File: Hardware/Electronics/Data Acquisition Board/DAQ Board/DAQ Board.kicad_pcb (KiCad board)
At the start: 4 copper layers, 94.7 x 58.9 mm, 133 parts, among them J1 Conn_01x09_Male, J10 ~CS~_TP, J12 START_TP, J14 MID_SUPPLY_TP, J15 AVDD_TP, J16 DVDD_TP, J2 USB_B_Mini, J4 DC Barrel Jack, J5 HC-05 BT Module, J6 ICSP Header, J7 VIN_RAW_TP, Q1 DMP2100U, SW10 SW_SPDT, SW11 SW_SPDT, SW2 SW_DIP_x02, SW3 SW_SPDT, SW4 SW_SPDT, SW5 SW_SPDT, SW6 SW_SPDT, SW7 SW_SPDT, SW8 SW_SPDT, SW9 SW_SPDT, U1 ATmega328P-AU, U2 MCP1755T-5002E_SOT223-5, U3 LM3480-3.3, U4 MCP1755T-5002E_SOT223-5, U5 FT232RL, Y1 16MHz

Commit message: moved some vias
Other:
- board text added: "POW"
- board text added: "STAT"
- board text removed: "POWER"
- board text removed: "STATUS"
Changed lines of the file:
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@@
     (thickness 1.6)
     (drawings 41)
-    (tracks 915)
+    (tracks 917)
     (zones 0)
     (modules 133)
@@
   (layers
     (0 F.Cu signal)
-    (1 In1.Cu power)
-    (2 In2.Cu jumper)
-    (31 B.Cu signal)
-    (32 B.Adhes user)
+    (1 In1.Cu power hide)
+    (2 In2.Cu jumper hide)
+    (31 B.Cu signal hide)
+    (32 B.Adhes user hide)
     (33 F.Adhes user)
-    (34 B.Paste user)
+    (34 B.Paste user hide)
     (35 F.Paste user)
-    (36 B.SilkS user)
+    (36 B.SilkS user hide)
     (37 F.SilkS user)
-    (38 B.Mask user)
+    (38 B.Mask user hide)
     (39 F.Mask user)
-    (40 Dwgs.User user)
-    (41 Cmts.User user)
-    (42 Eco1.User user)
-    (43 Eco2.User user)
-    (44 Edge.Cuts user)
-    (45 Margin user)
-    (46 B.CrtYd user)
+    (40 Dwgs.User user hide)
+    (41 Cmts.User user hide)
+    (42 Eco1.User user hide)
+    (43 Eco2.User user hide)
+    (44 Edge.Cuts user hide)
+    (45 Margin user hide)
+    (46 B.CrtYd user hide)
     (47 F.CrtYd user)
-    (48 B.Fab user)
+    (48 B.Fab user hide)
     (49 F.Fab user hide)
   )
@@
   (module Switches:1825910-6 (layer F.Cu)
     (at 184.54 117.95 270)
-    (fp_text reference PB1 (at -2.95 -0.75 270) (layer F.SilkS)
+    (fp_text reference PB1 (at 3.36 -1.53 270) (layer F.SilkS)
       (effects (font (size 1 1) (thickness 0.15)))
     )
@@
     (tags diode)
     (attr smd)
-    (fp_text reference D6 (at 2.8925 -0.02) (layer F.SilkS)
+    (fp_text reference D6 (at -2.6075 0) (layer F.SilkS)
       (effects (font (size 1 1) (thickness 0.15)))
     )
@@
     (tags capacitor)
     (attr smd)
-    (fp_text reference C13 (at 3.22 -0.02 90) (layer F.SilkS)
+    (fp_text reference C13 (at 3.051482 -0.020428 90) (layer F.SilkS)
       (effects (font (size 1 1) (thickness 0.15)))
     )
@@
     (tags capacitor)
     (attr smd)
-    (fp_text reference C26 (at 0.61 -1.88 -90) (layer F.SilkS)
+    (fp_text reference C26 (at 0.641482 -1.760428 -90) (layer F.SilkS)
       (effects (font (size 1 1) (thickness 0.15)))
     )
@@
     (tags capacitor)
     (attr smd)
-    (fp_text reference C55 (at -1.321415 1.611237) (layer F.SilkS)
+    (fp_text reference C55 (at -1.581843 2.379755) (layer F.SilkS)
       (effects (font (size 1 1) (thickness 0.15)))
     )
@@
     (tags diode)
     (attr smd)
-    (fp_text reference D4 (at 2.81 -0.02) (layer F.SilkS)
+    (fp_text reference D4 (at -2.69 0) (layer F.SilkS)
       (effects (font (size 1 1) (thickness 0.15)))
     )
@@
     (tags diode)
     (attr smd)
-    (fp_text reference D5 (at 2.83 -0.01) (layer F.SilkS)
+    (fp_text reference D5 (at -2.67 0.01) (layer F.SilkS)
       (effects (font (size 1 1) (thickness 0.15)))
     )
@@
     (descr "Barrel Jack, 2.0mm ID, 5.5mm OD, 24V, 8A, no switch, https://www.cui.com/product/resource/pj-063ah.pdf")
     (tags "barrel jack cui dc power")
-    (fp_text reference J4 (at 6.760428 12.191482 270) (layer F.SilkS)
+    (fp_text reference J4 (at -6.729572 0.261482 270) (layer F.SilkS)
       (effects (font (size 1 1) (thickness 0.15)))
     )
@@
     (tags SOT-23)
     (attr smd)
-    (fp_text reference Q1 (at 2.84 -0.63) (layer F.SilkS)
+    (fp_text reference Q1 (at 2.889572 -1.251482) (layer F.SilkS)
       (effects (font (size 1 1) (thickness 0.15)))
     )
@@
     (effects (font (size 1 1) (thickness 0.15)))
   )
-  (gr_text USB (at 140.790428 106.771482 180) (layer F.SilkS)
+  (gr_text USB (at 138.14 106.67) (layer F.SilkS)
     (effects (font (size 1 1) (thickness 0.15) italic) (justify left))
   )
-  (gr_text "BT\n" (at 135.420428 106.821482 180) (layer F.SilkS)
+  (gr_text "BT\n" (at 133.08 106.75) (layer F.SilkS)
     (effects (font (size 1 1) (thickness 0.15) italic) (justify left))
   )
@@
     (effects (font (size 1.5 1.5) (thickness 0.3)))
   )
-  (gr_text POWER (at 174.610428 111.591482) (layer F.SilkS)
+  (gr_text POW (at 184.403285 111.631482) (layer F.SilkS)
     (effects (font (size 1.5 1.5) (thickness 0.3)))
   )
-  (gr_text STATUS (at 174.450428 113.741482) (layer F.SilkS)
+  (gr_text STAT (at 184.510428 113.781482) (layer F.SilkS)
     (effects (font (size 1.5 1.5) (thickness 0.3)))
   )
@@
     (effects (font (size 1.5 1.5) (thickness 0.3)))
   )
-  (gr_text ADC (at 176.200428 115.901482) (layer F.SilkS)
+  (gr_text ADC (at 184.153285 115.941482) (layer F.SilkS)
     (effects (font (size 1.5 1.5) (thickness 0.3)))
   )
   (via (at 188.02 116.62) (size 0.8) (drill 0.4) (layers F.Cu B.Cu) (net 0))
+  (via (at 149.61 94.62) (size 0.8) (drill 0.4) (layers F.Cu B.Cu) (net 13))
+  (via (at 145.61 94.62) (size 0.8) (drill 0.4) (layers F.Cu B.Cu) (net 13))
+  (via (at 181.74 86.43) (size 0.8) (drill 0.4) (layers F.Cu B.Cu) (net 13))
+  (via (at 177.74 86.43) (size 0.8) (drill 0.4) (layers F.Cu B.Cu) (net 13))
   (segment (start 181.969687 72.654723) (end 181.972928 72.651482) (width 0.5) (layer F.Cu) (net 1))
   (segment (start 181.969687 74.238641) (end 181.969687 72.654723) (width 0.5) (layer F.Cu) (net 1))
@@
   (via (at 216.02 72.62) (size 0.8) (drill 0.4) (layers F.Cu B.Cu) (net 13))
   (via (at 220.02 72.62) (size 0.8) (drill 0.4) (layers F.Cu B.Cu) (net 13))
-  (via (at 136.02 76.62) (size 0.8) (drill 0.4) (layers F.Cu B.Cu) (net 13))
+  (via (at 137.59 76.5) (size 0.8) (drill 0.4) (layers F.Cu B.Cu) (net 13))
   (via (at 144.02 76.62) (size 0.8) (drill 0.4) (layers F.Cu B.Cu) (net 13))
   (via (at 148.02 76.62) (size 0.8) (drill 0.4) (layers F.Cu B.Cu) (net 13))
@@
   (via (at 220.02 100.62) (size 0.8) (drill 0.4) (layers F.Cu B.Cu) (net 13))
   (via (at 136.02 104.62) (size 0.8) (drill 0.4) (layers F.Cu B.Cu) (net 13))
-  (via (at 144.02 104.62) (size 0.8) (drill 0.4) (layers F.Cu B.Cu) (net 13))
   (via (at 160.02 104.62) (size 0.8) (drill 0.4) (layers F.Cu B.Cu) (net 13))
   (via (at 164.02 104.62) (size 0.8) (drill 0.4) (layers F.Cu B.Cu) (net 13))
@@
   (via (at 144.02 116.62) (size 0.8) (drill 0.4) (layers F.Cu B.Cu) (net 13))
   (via (at 148.02 116.62) (size 0.8) (drill 0.4) (layers F.Cu B.Cu) (net 13))
-  (via (at 152.02 116.62) (size 0.8) (drill 0.4) (layers F.Cu B.Cu) (net 13))
-  (via (at 156.02 116.62) (size 0.8) (drill 0.4) (layers F.Cu B.Cu) (net 13))
-  (via (at 160.02 116.62) (size 0.8) (drill 0.4) (layers F.Cu B.Cu) (net 13))
-  (via (at 164.02 116.62) (size 0.8) (drill 0.4) (layers F.Cu B.Cu) (net 13))
+  (via (at 151.21 116.58) (size 0.8) (drill 0.4) (layers F.Cu B.Cu) (net 13))
   (via (at 211.84 120.53) (size 0.8) (drill 0.4) (layers F.Cu B.Cu) (net 13))
   (via (at 207.78 116.69) (size 0.8) (drill 0.4) (layers F.Cu B.Cu) (net 13))
@@
   (via (at 135.16 94.83) (size 0.8) (drill 0.4) (layers F.Cu B.Cu) (net 36))
   (via (at 149.130428 104.161482) (size 0.8) (drill 0.4) (layers F.Cu B.Cu) (net 36))
-  (via (at 131.670428 77.141482) (size 0.8) (drill 0.4) (layers F.Cu B.Cu) (net 36))
-  (via (at 128.650428 77.141482) (size 0.8) (drill 0.4) (layers F.Cu B.Cu) (net 36))
+  (via (at 130.22 78.36) (size 0.8) (drill 0.4) (layers F.Cu B.Cu) (net 36))
+  (via (at 127.31 78.59) (size 0.8) (drill 0.4) (layers F.Cu B.Cu) (net 36))
   (via (at 134.770428 79.041482) (size 0.8) (drill 0.4) (layers F.Cu B.Cu) (net 36))
   (via (at 141.670428 81.671482) (size 0.8) (drill 0.4) (layers F.Cu B.Cu) (net 36))
@@
   (segment (start 134.79656 83.505179) (end 134.79656 85.609962) (width 0.5) (layer F.Cu) (net 36))
   (segment (start 131.670428 78.62133) (end 131.671843 78.622745) (width 0.5) (layer F.Cu) (net 36))
-  (segment (start 131.670428 77.141482) (end 131.670428 78.62133) (width 0.5) (layer F.Cu) (net 36))
   (segment (start 128.650428 78.613982) (end 128.680428 78.643982) (width 0.5) (layer F.Cu) (net 36))
-  (segment (start 128.650428 77.141482) (end 128.650428 78.613982) (width 0.5) (layer F.Cu) (net 36))
   (segment (start 147.377928 99.473982) (end 147.390428 99.461482) (width 0.5) (layer F.Cu) (net 36))
   (segment (start 147.377928 101.411482) (end 147.377928 99.473982) (width 0.5) (layer F.Cu) (net 36))
@@
   (segment (start 135.161482 94.831482) (end 135.16 94.83) (width 0.5) (layer F.Cu) (net 36))
   (segment (start 136.342928 94.831482) (end 135.161482 94.831482) (width 0.5) (layer F.Cu) (net 36))
+  (segment (start 127.363982 78.643982) (end 127.31 78.59) (width 0.5) (layer F.Cu) (net 36))
+  (segment (start 128.680428 78.643982) (end 127.363982 78.643982) (width 0.5) (layer F.Cu) (net 36))
+  (segment (start 131.409098 78.36) (end 131.671843 78.622745) (width 0.5) (layer F.Cu) (net 36))
+  (segment (start 130.22 78.36) (end 131.409098 78.36) (width 0.5) (layer F.Cu) (net 36))
   (via (at 152.280428 68.081482) (size 0.8) (drill 0.4) (layers F.Cu B.Cu) (net 37))
   (via (at 186.910428 111.061482) (size 0.8) (drill 0.4) (layers F.Cu B.Cu) (net 37))

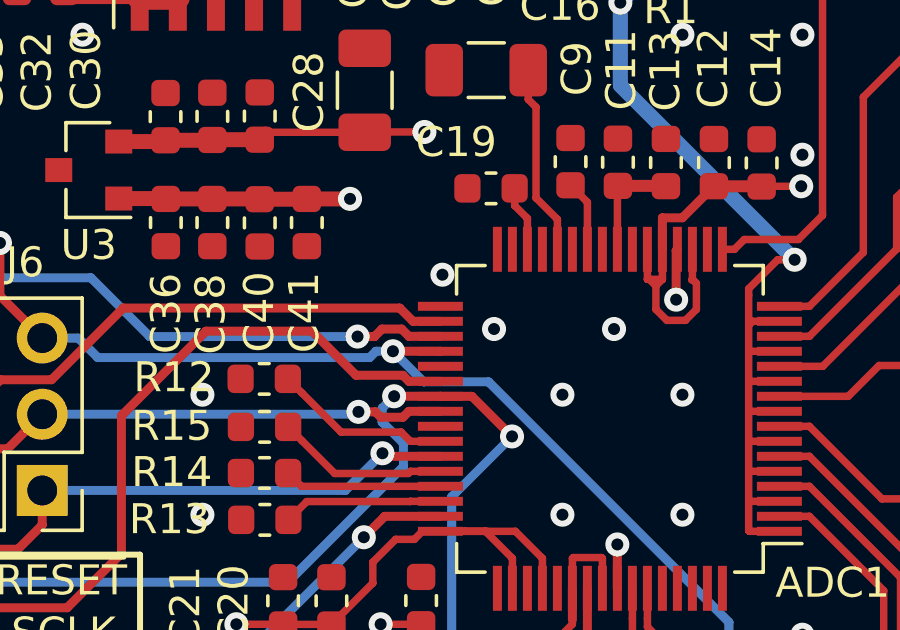
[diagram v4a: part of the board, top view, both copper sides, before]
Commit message: Added pullup to ADS1299 CS pin
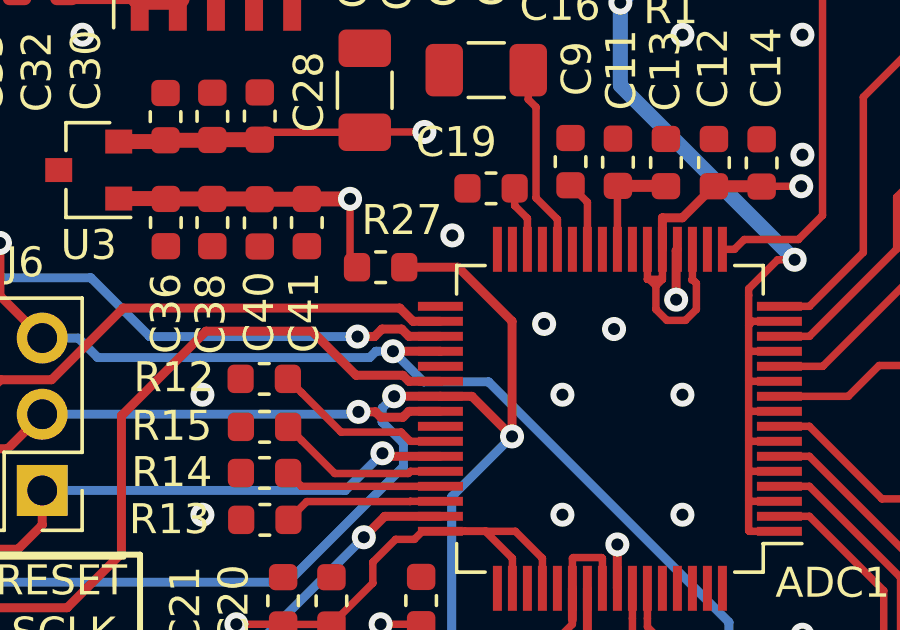
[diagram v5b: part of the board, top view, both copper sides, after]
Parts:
- added R27: 100k, Resistor_SMD:R_0603_1608Metric, F.Cu at (174.0, 84.4)
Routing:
- net /~CS: track 60.5 -> 68.7 mm
- net /ADC1299/DVDD: track 59.8 -> 62.2 mm
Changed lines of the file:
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@@
     (thickness 1.6)
     (drawings 41)
-    (tracks 917)
+    (tracks 922)
     (zones 0)
-    (modules 133)
+    (modules 134)
     (nets 113)
   )
@@
   (layers
     (0 F.Cu signal)
-    (1 In1.Cu power hide)
-    (2 In2.Cu jumper hide)
-    (31 B.Cu signal hide)
-    (32 B.Adhes user hide)
+    (1 In1.Cu power)
+    (2 In2.Cu jumper)
+    (31 B.Cu signal)
+    (32 B.Adhes user)
     (33 F.Adhes user)
-    (34 B.Paste user hide)
+    (34 B.Paste user)
     (35 F.Paste user)
-    (36 B.SilkS user hide)
+    (36 B.SilkS user)
     (37 F.SilkS user)
-    (38 B.Mask user hide)
+    (38 B.Mask user)
     (39 F.Mask user)
-    (40 Dwgs.User user hide)
-    (41 Cmts.User user hide)
-    (42 Eco1.User user hide)
+    (40 Dwgs.User user)
+    (41 Cmts.User user)
+    (42 Eco1.User user)
     (43 Eco2.User user hide)
-    (44 Edge.Cuts user hide)
-    (45 Margin user hide)
-    (46 B.CrtYd user hide)
+    (44 Edge.Cuts user)
+    (45 Margin user)
+    (46 B.CrtYd user)
     (47 F.CrtYd user)
     (48 B.Fab user hide)
@@
     (add_net "/Arduino Nano/VUSB")
   )
+  (module Resistor_SMD:R_0603_1608Metric (layer F.Cu)
+    (at 173.96 84.37)
+    (descr "Resistor SMD 0603 (1608 Metric), square (rectangular) end terminal, IPC_7351 nominal, (Body size source: http://www.tortai-tech.com/upload/download/2011102023233369053.pdf), generated with kicad-footprint-generator")
+    (tags resistor)
+    (attr smd)
+    (fp_text reference R27 (at 0.71 -1.57) (layer F.SilkS)
+      (effects (font (size 1 1) (thickness 0.15)))
+    )
+    (fp_text value 100k (at 0 1.43) (layer F.Fab)
+      (effects (font (size 1 1) (thickness 0.15)))
+    )
+    (fp_line (start -0.8 0.4) (end -0.8 -0.4) (layer F.Fab) (width 0.1))
+    (fp_line (start -0.8 -0.4) (end 0.8 -0.4) (layer F.Fab) (width 0.1))
+    (fp_line (start 0.8 -0.4) (end 0.8 0.4) (layer F.Fab) (width 0.1))
+    (fp_line (start 0.8 0.4) (end -0.8 0.4) (layer F.Fab) (width 0.1))
+    (fp_line (start -0.162779 -0.51) (end 0.162779 -0.51) (layer F.SilkS) (width 0.12))
+    (fp_line (start -0.162779 0.51) (end 0.162779 0.51) (layer F.SilkS) (width 0.12))
+    (fp_line (start -1.48 0.73) (end -1.48 -0.73) (layer F.CrtYd) (width 0.05))
+    (fp_line (start -1.48 -0.73) (end 1.48 -0.73) (layer F.CrtYd) (width 0.05))
+    (fp_line (start 1.48 -0.73) (end 1.48 0.73) (layer F.CrtYd) (width 0.05))
+    (fp_line (start 1.48 0.73) (end -1.48 0.73) (layer F.CrtYd) (width 0.05))
+    (fp_text user %R (at 0 0) (layer F.Fab)
+      (effects (font (size 0.4 0.4) (thickness 0.06)))
+    )
+    (pad 1 smd roundrect (at -0.7875 0) (size 0.875 0.95) (layers F.Cu F.Paste F.Mask) (roundrect_rratio 0.25)
+      (net 28 /ADC1299/DVDD))
+    (pad 2 smd roundrect (at 0.7875 0) (size 0.875 0.95) (layers F.Cu F.Paste F.Mask) (roundrect_rratio 0.25)
+      (net 111 /~CS))
+    (model ${KISYS3DMOD}/Resistor_SMD.3dshapes/R_0603_1608Metric.wrl
+      (at (xyz 0 0 0))
+      (scale (xyz 1 1 1))
+      (rotate (xyz 0 0 0))
+    )
+  )
   (module Capacitor_SMD:C_0603_1608Metric (layer F.Cu)
     (at 141.61 92.75 90)
@@
   (via (at 145.61 94.62) (size 0.8) (drill 0.4) (layers F.Cu B.Cu) (net 13))
   (via (at 181.74 86.43) (size 0.8) (drill 0.4) (layers F.Cu B.Cu) (net 13))
-  (via (at 177.74 86.43) (size 0.8) (drill 0.4) (layers F.Cu B.Cu) (net 13))
+  (via (at 179.41 86.26) (size 0.8) (drill 0.4) (layers F.Cu B.Cu) (net 13))
   (segment (start 181.969687 72.654723) (end 181.972928 72.651482) (width 0.5) (layer F.Cu) (net 1))
   (segment (start 181.969687 74.238641) (end 181.969687 72.654723) (width 0.5) (layer F.Cu) (net 1))
@@
   (via (at 148.02 84.62) (size 0.8) (drill 0.4) (layers F.Cu B.Cu) (net 13))
   (via (at 152.02 84.62) (size 0.8) (drill 0.4) (layers F.Cu B.Cu) (net 13))
-  (via (at 176.02 84.62) (size 0.8) (drill 0.4) (layers F.Cu B.Cu) (net 13))
+  (via (at 176.35 83.31) (size 0.8) (drill 0.4) (layers F.Cu B.Cu) (net 13))
   (via (at 200.02 84.62) (size 0.8) (drill 0.4) (layers F.Cu B.Cu) (net 13))
   (via (at 220.02 84.62) (size 0.8) (drill 0.4) (layers F.Cu B.Cu) (net 13))
@@
   (segment (start 175.952928 93.173482) (end 176.750428 93.173482) (width 0.25) (layer F.Cu) (net 28))
   (segment (start 176.750428 93.173482) (end 177.50293 93.173482) (width 0.25) (layer F.Cu) (net 28))
+  (segment (start 172.940428 84.137928) (end 173.1725 84.37) (width 0.25) (layer F.Cu) (net 28))
+  (segment (start 172.940428 82.091482) (end 172.940428 84.137928) (width 0.25) (layer F.Cu) (net 28))
   (segment (start 180.477928 99.211482) (end 180.477928 97.611482) (width 0.4) (layer F.Cu) (net 29))
   (segment (start 180.852928 97.236482) (end 180.852928 95.073482) (width 0.3) (layer F.Cu) (net 29))
@@
   (segment (start 172.924315 106.56) (end 172.204314 107.280001) (width 0.3) (layer F.Cu) (net 111))
   (segment (start 173.49 106.56) (end 172.924315 106.56) (width 0.3) (layer F.Cu) (net 111))
+  (segment (start 178.340428 86.170428) (end 178.340428 90.010982) (width 0.3) (layer F.Cu) (net 111))
+  (segment (start 174.7475 84.37) (end 176.54 84.37) (width 0.3) (layer F.Cu) (net 111))
+  (segment (start 176.54 84.37) (end 178.340428 86.170428) (width 0.3) (layer F.Cu) (net 111))
   (via (at 161.270428 83.561482) (size 0.8) (drill 0.4) (layers F.Cu B.Cu) (net 112))
   (via (at 174.370428 87.171482) (size 0.8) (drill 0.4) (layers F.Cu B.Cu) (net 112))
@@
     (polygon
       (pts
-        (xy 222.010428 126.601482) (xy 171.550428 126.671482) (xy 171.530428 103.081482) (xy 164.780428 102.771482) (xy 164.730428 85.191482)
+        (xy 222.010428 126.601482) (xy 171.550428 126.671482) (xy 171.530428 103.081482) (xy 164.84 103.1) (xy 164.730428 85.191482)
         (xy 158.240428 85.291482) (xy 158.150428 78.851482) (xy 148.340428 79.001482) (xy 148.340428 65.591482) (xy 162.090428 65.581482)
         (xy 162.110428 76.761482) (xy 164.220428 76.721482) (xy 164.260428 83.621482) (xy 168.240428 83.631482) (xy 168.170428 85.511482)
@@
     (polygon
       (pts
-        (xy 166.92 108.12) (xy 178.44 108.06) (xy 178.41 131.32) (xy 166.98 131.4)
+        (xy 165.74 108.1) (xy 178.44 108.06) (xy 178.41 131.32) (xy 165.8 131.38)
       )
     )

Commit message: ran DRC
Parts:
- added J11: Conn_01x01_Male, Sparker:DIN 42802-1, F.Cu at (226.1, 96.4)
- added J13: Conn_01x01_Male, Sparker:DIN 42802-1, F.Cu at (217.2, 90.3)
- added J17: Conn_01x01_Male, Sparker:DIN 42802-1, F.Cu at (226.1, 84.3)
- added J18: Conn_01x01_Male, Sparker:DIN 42802-1, F.Cu at (217.2, 78.2)
- added J19: Conn_01x01_Male, Sparker:DIN 42802-1, F.Cu at (226.1, 72.2)
- added J3: Conn_01x01_Male, Sparker:DIN 42802-1, F.Cu at (217.2, 114.5)
- added J8: Conn_01x01_Male, Sparker:DIN 42802-1, F.Cu at (226.1, 108.5)
- added J9: Conn_01x01_Male, Sparker:DIN 42802-1, F.Cu at (217.2, 102.4)
- F1: value 0251004.NRT1L -> 025101.5MAT1L
- J1: value Conn_01x09_Male -> Conn_01x01_Male; footprint Connectors:TE-5-103669-8 -> Sparker:DIN 42802-1
- moved J1 22.4 mm to (226.1, 120.6)
- moved MH4 11.2 mm to (148.9, 123.0)
- moved LOGO1 4.62 mm to (207.6, 114.7)
- moved MH1 1.15 mm to (216.1, 123.0)
- moved MH2 1.07 mm to (216.2, 70.0)
- moved MH3 0.82 mm to (130.4, 70.0)
- turned J10 to 90 degrees
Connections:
- SW10 pad 3: Net-(J1-Pad8) -> Net-(J18-Pad1)
- SW11 pad 3: Net-(J1-Pad9) -> Net-(J19-Pad1)
- SW4 pad 3: Net-(J1-Pad2) -> Net-(J3-Pad1)
- SW5 pad 3: Net-(J1-Pad3) -> Net-(J8-Pad1)
- SW6 pad 3: Net-(J1-Pad4) -> Net-(J9-Pad1)
- SW7 pad 3: Net-(J1-Pad5) -> Net-(J11-Pad1)
- SW8 pad 3: Net-(J1-Pad6) -> Net-(J13-Pad1)
- SW9 pad 3: Net-(J1-Pad7) -> Net-(J17-Pad1)
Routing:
- net Net-(J8-Pad1): track 0.00 -> 21.8 mm
- net Net-(J11-Pad1): track 0.00 -> 21.2 mm
- net Net-(J17-Pad1): track 0.00 -> 19.2 mm
- net Net-(J19-Pad1): track 0.00 -> 17.9 mm
- net Net-(J3-Pad1): track 0.00 -> 15.3 mm
- net Net-(J1-Pad9): track 13.9 -> 0.00 mm
- net Net-(J9-Pad1): track 0.00 -> 13.0 mm
- net Net-(J1-Pad8): track 12.1 -> 0.00 mm
- net Net-(J1-Pad2): track 12.0 -> 0.00 mm
- net Net-(J1-Pad1): track 13.5 -> 24.8 mm
- net Net-(J1-Pad7): track 11.2 -> 0.00 mm
- net Net-(J1-Pad3): track 11.2 -> 0.00 mm
- net Net-(J13-Pad1): track 0.00 -> 11.0 mm
- net Net-(J1-Pad6): track 10.4 -> 0.00 mm
- net Net-(J1-Pad4): track 10.4 -> 0.00 mm
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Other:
- board size 94.7 x 58.9 mm -> 105.4 x 58.9 mm
